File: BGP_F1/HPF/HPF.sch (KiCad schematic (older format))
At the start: 14 parts, among them P1 CONN_01X05, P2 CONN_01X06, U1 MC33178

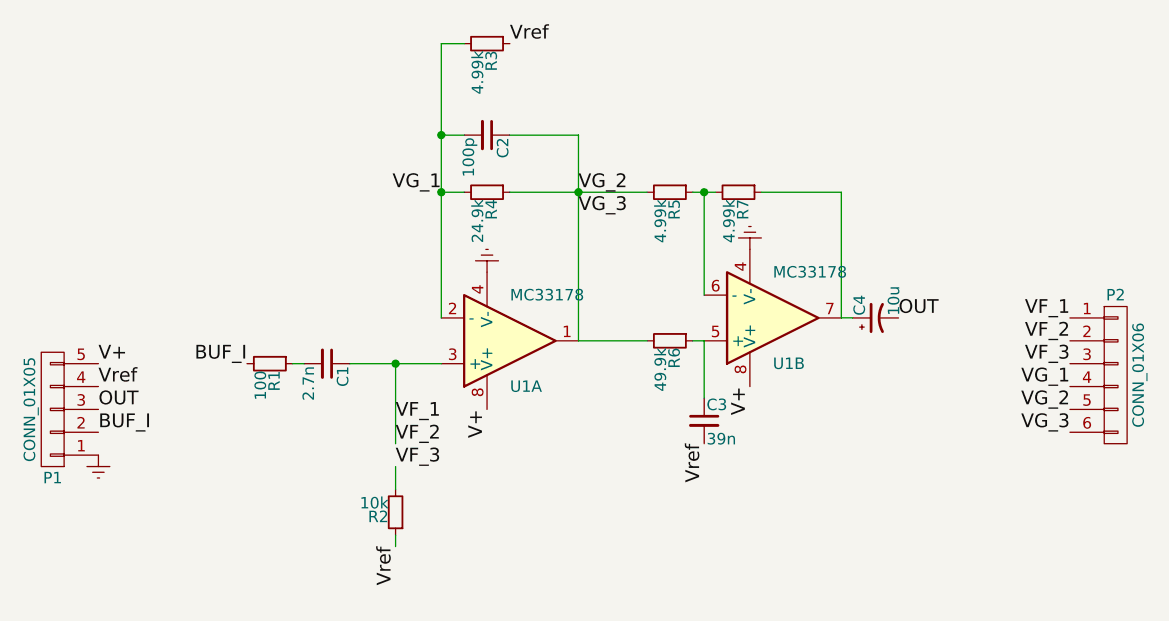
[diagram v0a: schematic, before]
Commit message: F boards routed, various optimisations made
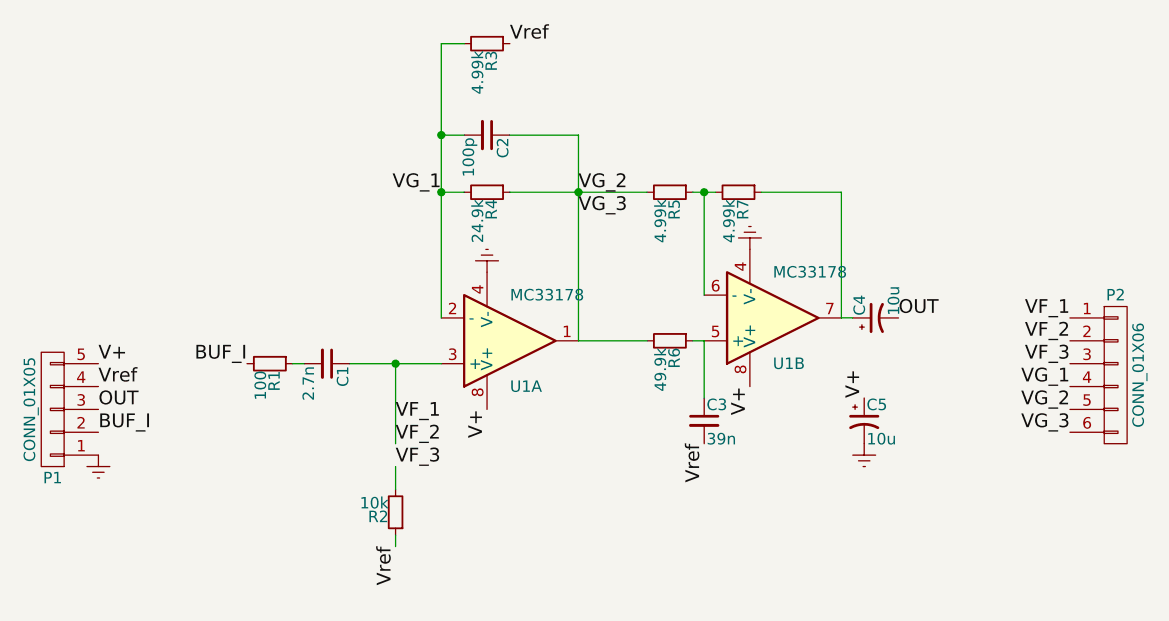
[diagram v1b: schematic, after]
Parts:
- added C5: 10u, Capacitors_Tantalum_SMD:TantalC_SizeR_EIA-2012, symbol CP1_Small
- R1, R2, R3, R4, R5, R6, R7: footprint Resistors_SMD:R_0805_HandSoldering -> Resistors_SMD:R_0603_HandSoldering
- U1: footprint Housings_SSOP:MSOP-8_3x3mm_Pitch0.65mm -> Housings_SOIC:SOIC-8_3.9x4.9mm_Pitch1.27mm
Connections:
- net Earth: now also C5.2
- net V+: now also C5.1
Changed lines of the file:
@@
 F 0 "R1" H 4280 3820 50  0000 L CNN
 F 1 "100" H 4280 3760 50  0000 L CNN
-F 2 "Resistors_SMD:R_0805_HandSoldering" H 4250 3800 50  0001 C CNN
+F 2 "Resistors_SMD:R_0603_HandSoldering" H 4250 3800 50  0001 C CNN
 F 3 "" H 4250 3800 50  0000 C CNN
 	1    4250 3800
@@
 F 0 "R2" H 4830 4470 50  0000 L CNN
 F 1 "10k" H 4830 4410 50  0000 L CNN
-F 2 "Resistors_SMD:R_0805_HandSoldering" H 4800 4450 50  0001 C CNN
+F 2 "Resistors_SMD:R_0603_HandSoldering" H 4800 4450 50  0001 C CNN
 F 3 "" H 4800 4450 50  0000 C CNN
 	1    4800 4450
@@
 F 0 "U1" H 5300 3900 50  0000 L CNN
 F 1 "MC33178" H 5300 3500 50  0000 L CNN
-F 2 "Housings_SSOP:MSOP-8_3x3mm_Pitch0.65mm" H 5200 3750 50  0001 C CNN
+F 2 "Housings_SOIC:SOIC-8_3.9x4.9mm_Pitch1.27mm" H 5200 3750 50  0001 C CNN
 F 3 "" H 5300 3850 50  0000 C CNN
 	1    5300 3700
@@
 V+
 $Comp
-L Earth #PWR01
+L Earth #PWR2
 U 1 1 5A5EB367
 P 5200 3400
-F 0 "#PWR01" H 5200 3150 50  0001 C CNN
+F 0 "#PWR2" H 5200 3150 50  0001 C CNN
 F 1 "Earth" H 5200 3250 50  0001 C CNN
 F 2 "" H 5200 3400 50  0000 C CNN
@@
 F 0 "R4" H 5230 3070 50  0000 L CNN
 F 1 "24.9k" H 5230 3010 50  0000 L CNN
-F 2 "Resistors_SMD:R_0805_HandSoldering" H 5200 3050 50  0001 C CNN
+F 2 "Resistors_SMD:R_0603_HandSoldering" H 5200 3050 50  0001 C CNN
 F 3 "" H 5200 3050 50  0000 C CNN
 	1    5200 3050
@@
 F 0 "R3" H 5230 2420 50  0000 L CNN
 F 1 "4.99k" H 5230 2360 50  0000 L CNN
-F 2 "Resistors_SMD:R_0805_HandSoldering" H 5200 2400 50  0001 C CNN
+F 2 "Resistors_SMD:R_0603_HandSoldering" H 5200 2400 50  0001 C CNN
 F 3 "" H 5200 2400 50  0000 C CNN
 	1    5200 2400
@@
 F 0 "R5" H 6030 3070 50  0000 L CNN
 F 1 "4.99k" H 6030 3010 50  0000 L CNN
-F 2 "Resistors_SMD:R_0805_HandSoldering" H 6000 3050 50  0001 C CNN
+F 2 "Resistors_SMD:R_0603_HandSoldering" H 6000 3050 50  0001 C CNN
 F 3 "" H 6000 3050 50  0000 C CNN
 	1    6000 3050
@@
 F 0 "R7" H 6330 3070 50  0000 L CNN
 F 1 "4.99k" H 6330 3010 50  0000 L CNN
-F 2 "Resistors_SMD:R_0805_HandSoldering" H 6300 3050 50  0001 C CNN
+F 2 "Resistors_SMD:R_0603_HandSoldering" H 6300 3050 50  0001 C CNN
 F 3 "" H 6300 3050 50  0000 C CNN
 	1    6300 3050
@@
 F 0 "U1" H 6450 3800 50  0000 L CNN
 F 1 "MC33178" H 6450 3400 50  0000 L CNN
-F 2 "Housings_SSOP:MSOP-8_3x3mm_Pitch0.65mm" H 6350 3650 50  0001 C CNN
+F 2 "Housings_SOIC:SOIC-8_3.9x4.9mm_Pitch1.27mm" H 6350 3650 50  0001 C CNN
 F 3 "" H 6450 3750 50  0000 C CNN
 	2    6450 3600
@@
 F 0 "R6" H 6030 3720 50  0000 L CNN
 F 1 "49.9k" H 6030 3660 50  0000 L CNN
-F 2 "Resistors_SMD:R_0805_HandSoldering" H 6000 3700 50  0001 C CNN
+F 2 "Resistors_SMD:R_0603_HandSoldering" H 6000 3700 50  0001 C CNN
 F 3 "" H 6000 3700 50  0000 C CNN
 	1    6000 3700
@@
 OUT
 $Comp
-L Earth #PWR02
+L Earth #PWR3
 U 1 1 5A5EBD48
 P 6350 3300
-F 0 "#PWR02" H 6350 3050 50  0001 C CNN
+F 0 "#PWR3" H 6350 3050 50  0001 C CNN
 F 1 "Earth" H 6350 3150 50  0001 C CNN
 F 2 "" H 6350 3300 50  0000 C CNN
@@
 OUT
 $Comp
-L Earth #PWR03
+L Earth #PWR1
 U 1 1 5A5EC171
 P 3500 4200
-F 0 "#PWR03" H 3500 3950 50  0001 C CNN
+F 0 "#PWR1" H 3500 3950 50  0001 C CNN
 F 1 "Earth" H 3500 4050 50  0001 C CNN
 F 2 "" H 3500 4200 50  0000 C CNN
@@
 Text Label 7750 4100 2    60   ~ 0
 VG_3
+$Comp
+L CP1_Small C5
+U 1 1 5A5FF012
+P 6850 4050
+F 0 "C5" H 6860 4120 50  0000 L CNN
+F 1 "10u" H 6860 3970 50  0000 L CNN
+F 2 "Capacitors_Tantalum_SMD:TantalC_SizeR_EIA-2012" H 6850 4050 50  0001 C CNN
+F 3 "" H 6850 4050 50  0000 C CNN
+	1    6850 4050
+	1    0    0    -1
+$EndComp
+Text Label 6850 3950 1    60   ~ 0
+V+
+$Comp
+L Earth #PWR4
+U 1 1 5A5FF0A6
+P 6850 4150
+F 0 "#PWR4" H 6850 3900 50  0001 C CNN
+F 1 "Earth" H 6850 4000 50  0001 C CNN
+F 2 "" H 6850 4150 50  0000 C CNN
+F 3 "" H 6850 4150 50  0000 C CNN
+	1    6850 4150
+	1    0    0    -1
+$EndComp
 $EndSCHEMATC

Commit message: Flipped boards so that they should be facing the right way
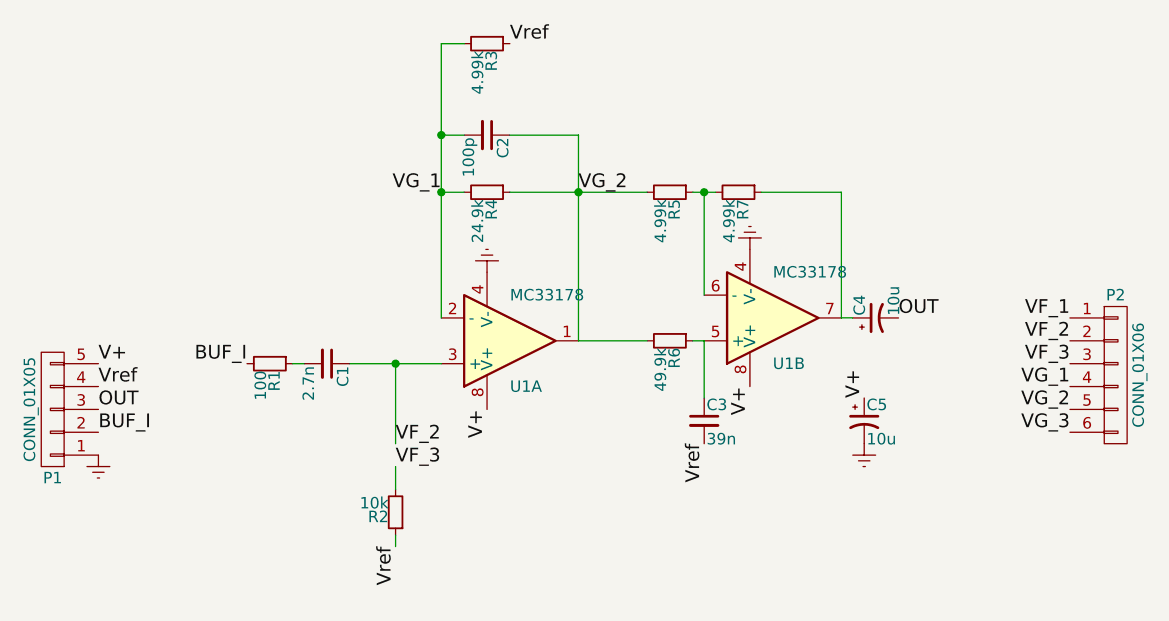
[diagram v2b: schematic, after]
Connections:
- net VF_1: no longer C1.1, P2.2 (P2), U1.3 (+)
- net VG_2: no longer P2.6 (P6)
- new net VF_2: C1.1, P2.2 (P2), U1.3 (+)
- new net VG_3: P2.6 (P6)
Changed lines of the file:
@@
 	-1   0    0    1
 $EndComp
-Text Label 4800 4050 0    60   ~ 0
-VF_1
 Text Label 4800 4150 0    60   ~ 0
 VF_2
@@
 Text Label 5600 3050 0    60   ~ 0
 VG_2
-Text Label 5600 3150 0    60   ~ 0
-VG_3
 Text Label 4150 3800 2    60   ~ 0
 BUF_I

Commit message: Pot tinkering
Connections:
- net VG_1: no longer C2.2, R3.2, R4.2, U1.2 (-)
- net VG_2: now also C2.2, R3.2, R4.2, U1.2 (-); no longer C2.1, R4.1, R5.2, R6.2, U1.1
- net VG_3: now also C2.1, R4.1, R5.2, R6.2, U1.1
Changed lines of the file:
@@
 V+
 $Comp
-L Earth #PWR2
+L Earth #PWR01
 U 1 1 5A5EB367
 P 5200 3400
-F 0 "#PWR2" H 5200 3150 50  0001 C CNN
+F 0 "#PWR01" H 5200 3150 50  0001 C CNN
 F 1 "Earth" H 5200 3250 50  0001 C CNN
 F 2 "" H 5200 3400 50  0000 C CNN
@@
 Text Label 5300 2400 0    60   ~ 0
 Vref
-Text Label 5000 3050 2    60   ~ 0
-VG_1
-Text Label 5600 3050 0    60   ~ 0
+Text Label 5600 2800 0    60   ~ 0
+VG_3
+Text Label 5000 2800 2    60   ~ 0
 VG_2
 Text Label 4150 3800 2    60   ~ 0
@@
 OUT
 $Comp
-L Earth #PWR3
+L Earth #PWR02
 U 1 1 5A5EBD48
 P 6350 3300
-F 0 "#PWR3" H 6350 3050 50  0001 C CNN
+F 0 "#PWR02" H 6350 3050 50  0001 C CNN
 F 1 "Earth" H 6350 3150 50  0001 C CNN
 F 2 "" H 6350 3300 50  0000 C CNN
@@
 OUT
 $Comp
-L Earth #PWR1
+L Earth #PWR03
 U 1 1 5A5EC171
 P 3500 4200
-F 0 "#PWR1" H 3500 3950 50  0001 C CNN
+F 0 "#PWR03" H 3500 3950 50  0001 C CNN
 F 1 "Earth" H 3500 4050 50  0001 C CNN
 F 2 "" H 3500 4200 50  0000 C CNN
@@
 V+
 $Comp
-L Earth #PWR4
+L Earth #PWR04
 U 1 1 5A5FF0A6
 P 6850 4150
-F 0 "#PWR4" H 6850 3900 50  0001 C CNN
+F 0 "#PWR04" H 6850 3900 50  0001 C CNN
 F 1 "Earth" H 6850 4000 50  0001 C CNN
 F 2 "" H 6850 4150 50  0000 C CNN

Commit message: New F0 Version
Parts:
- P1: footprint Connectors_Molex:Molex_MicroLatch-53253-0570_05x2.00mm_Straight -> Connectors_JST:JST_PH_B5B-PH-K_05x2.00mm_Straight
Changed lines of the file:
@@
 F 0 "P1" H 3300 4300 50  0000 C CNN
 F 1 "CONN_01X05" V 3400 4000 50  0000 C CNN
-F 2 "Connectors_Molex:Molex_MicroLatch-53253-0570_05x2.00mm_Straight" H 3300 4000 50  0001 C CNN
+F 2 "Connectors_JST:JST_PH_B5B-PH-K_05x2.00mm_Straight" H 3300 4000 50  0001 C CNN
 F 3 "" H 3300 4000 50  0000 C CNN
 	1    3300 4000

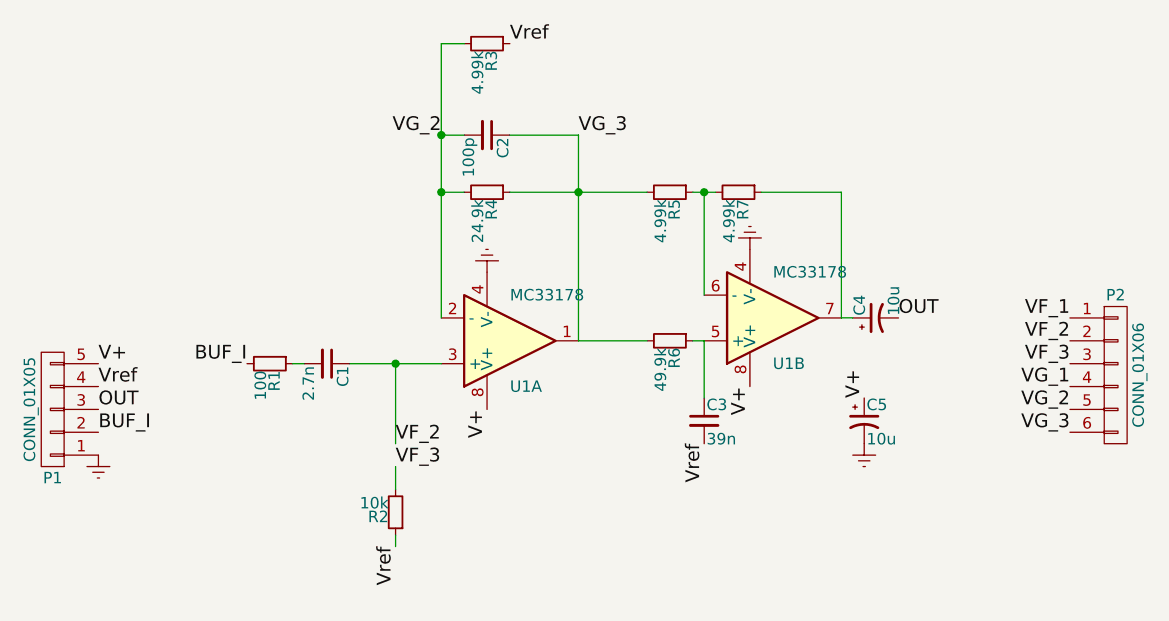
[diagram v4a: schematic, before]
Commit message: F1 updates to reverse pots
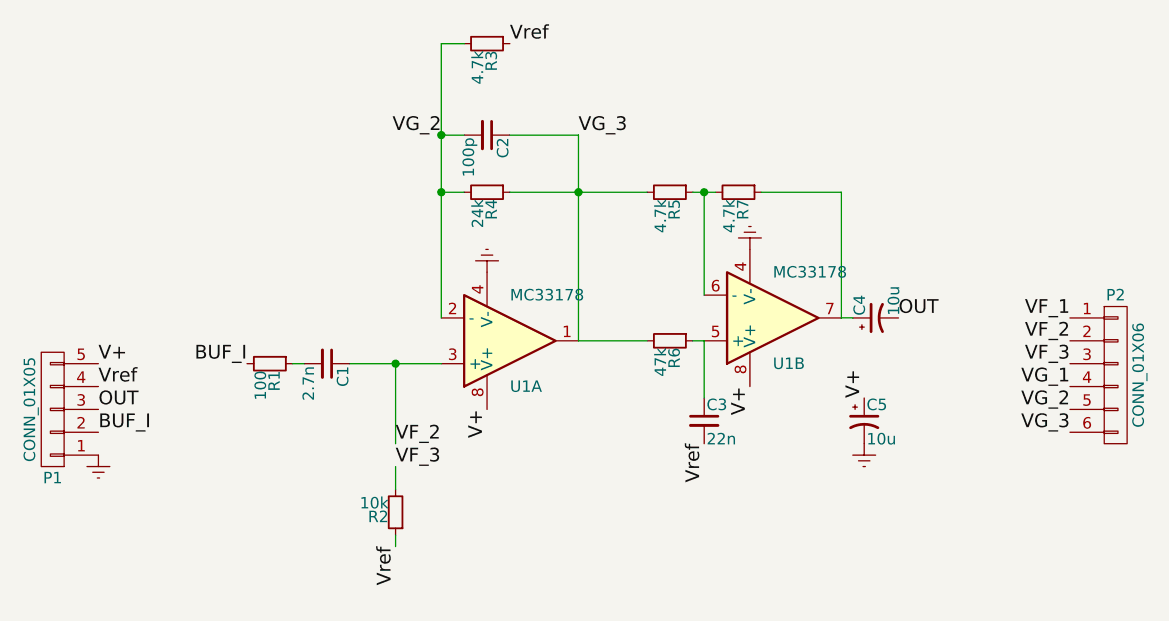
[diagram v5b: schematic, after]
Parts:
- C3: value 39n -> 22n
- R3, R5, R7: value 4.99k -> 4.7k
- R4: value 24.9k -> 24k
- R6: value 49.9k -> 47k
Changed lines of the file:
@@
 P 5200 3050
 F 0 "R4" H 5230 3070 50  0000 L CNN
-F 1 "24.9k" H 5230 3010 50  0000 L CNN
+F 1 "24k" H 5230 3010 50  0000 L CNN
 F 2 "Resistors_SMD:R_0603_HandSoldering" H 5200 3050 50  0001 C CNN
 F 3 "" H 5200 3050 50  0000 C CNN
@@
 P 5200 2400
 F 0 "R3" H 5230 2420 50  0000 L CNN
-F 1 "4.99k" H 5230 2360 50  0000 L CNN
+F 1 "4.7k" H 5230 2360 50  0000 L CNN
 F 2 "Resistors_SMD:R_0603_HandSoldering" H 5200 2400 50  0001 C CNN
 F 3 "" H 5200 2400 50  0000 C CNN
@@
 P 6000 3050
 F 0 "R5" H 6030 3070 50  0000 L CNN
-F 1 "4.99k" H 6030 3010 50  0000 L CNN
+F 1 "4.7k" H 6030 3010 50  0000 L CNN
 F 2 "Resistors_SMD:R_0603_HandSoldering" H 6000 3050 50  0001 C CNN
 F 3 "" H 6000 3050 50  0000 C CNN
@@
 P 6300 3050
 F 0 "R7" H 6330 3070 50  0000 L CNN
-F 1 "4.99k" H 6330 3010 50  0000 L CNN
+F 1 "4.7k" H 6330 3010 50  0000 L CNN
 F 2 "Resistors_SMD:R_0603_HandSoldering" H 6300 3050 50  0001 C CNN
 F 3 "" H 6300 3050 50  0000 C CNN
@@
 P 6000 3700
 F 0 "R6" H 6030 3720 50  0000 L CNN
-F 1 "49.9k" H 6030 3660 50  0000 L CNN
+F 1 "47k" H 6030 3660 50  0000 L CNN
 F 2 "Resistors_SMD:R_0603_HandSoldering" H 6000 3700 50  0001 C CNN
 F 3 "" H 6000 3700 50  0000 C CNN
@@
 P 6150 4050
 F 0 "C3" H 6160 4120 50  0000 L CNN
-F 1 "39n" H 6160 3970 50  0000 L CNN
+F 1 "22n" H 6160 3970 50  0000 L CNN
 F 2 "Capacitors_SMD:C_1206_HandSoldering" H 6150 4050 50  0001 C CNN
 F 3 "" H 6150 4050 50  0000 C CNN
